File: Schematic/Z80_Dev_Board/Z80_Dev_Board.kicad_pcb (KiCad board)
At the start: 2 copper layers, 120.7 x 98.3 mm, 45 parts, among them J1 MCU Interface, J2 MCU Interface 2, J3 Expansion port, J4 UART B, J5 UART A, J6 GPIO Input, J7 GPIO Output, U1 74AC08, U2 62256, U3 62256, U4 74AC00, U5 74AC04, U6 Z80 CPU, U7 74HC157, U8 74AC74, U9 SC26C92, X1 4MHz, Y1 3,6864 MHz

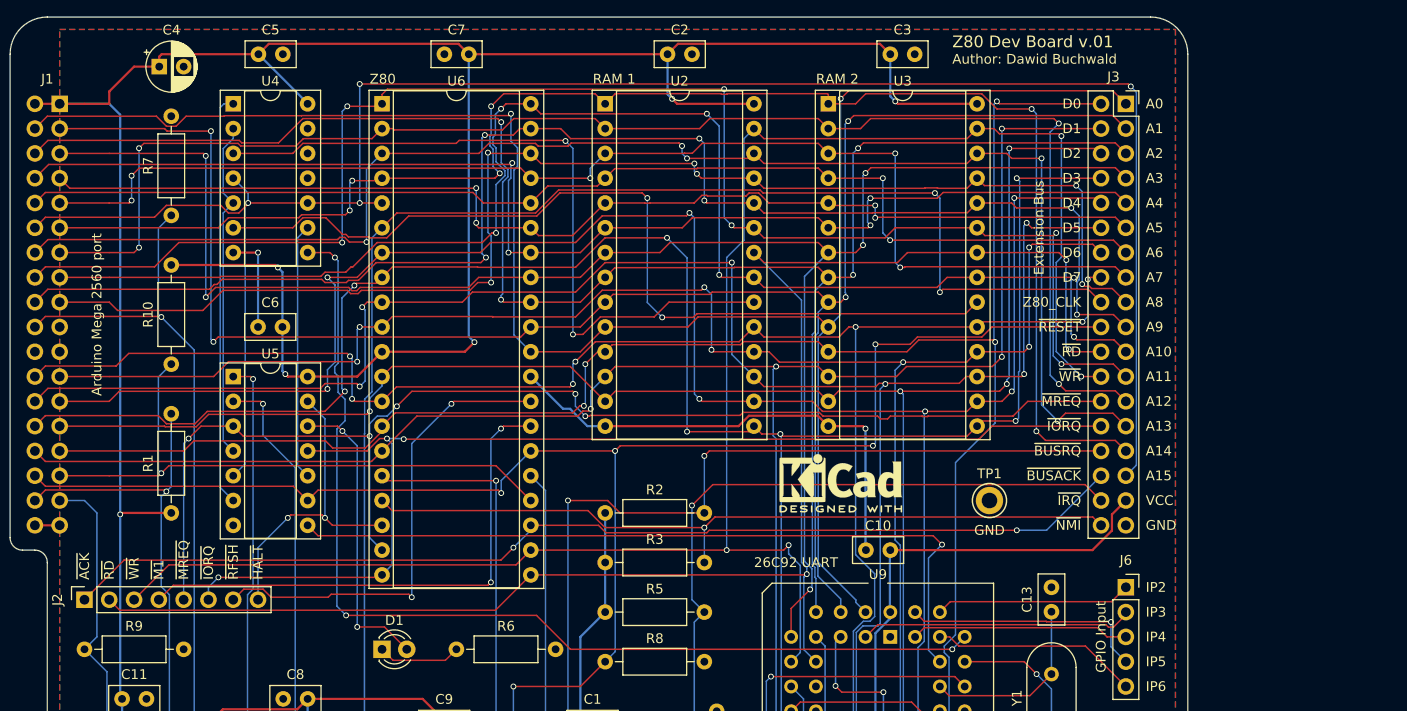
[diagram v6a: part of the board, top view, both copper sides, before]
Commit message: Started working on updated PCB with IO decoder
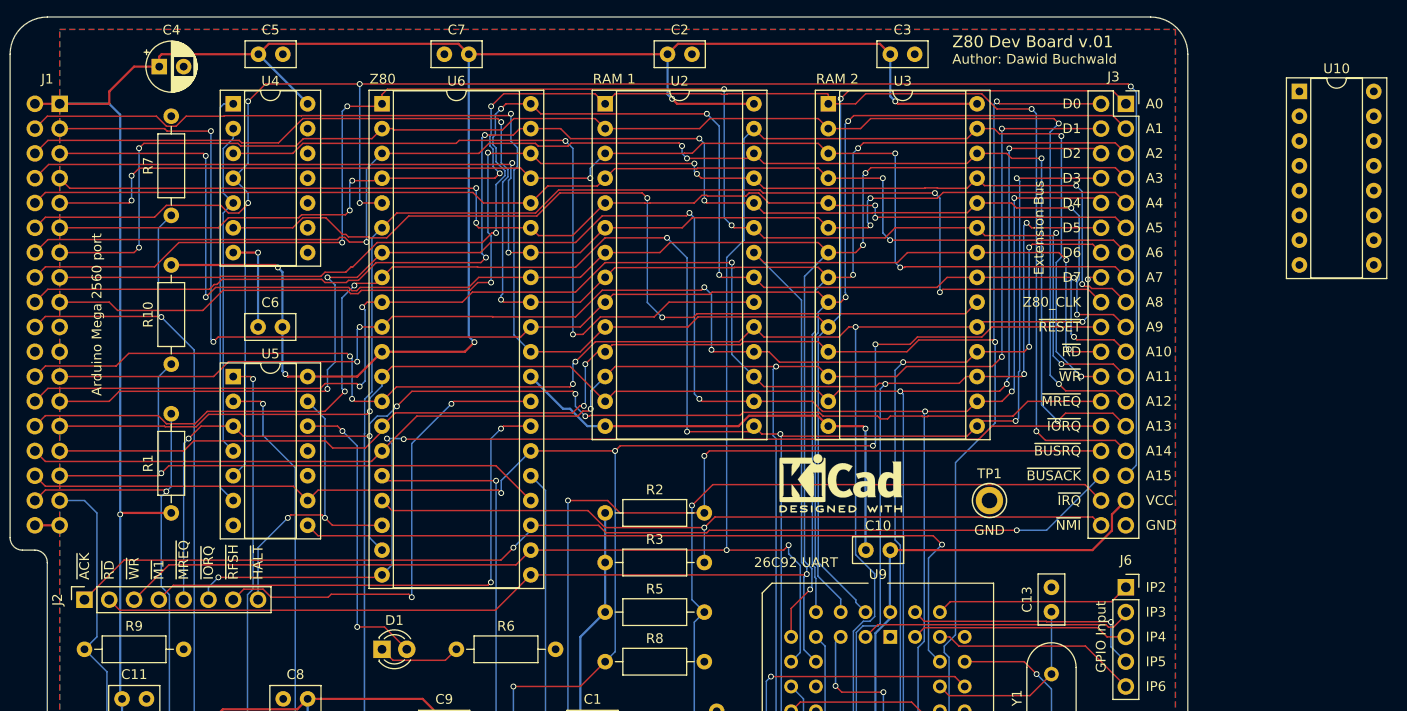
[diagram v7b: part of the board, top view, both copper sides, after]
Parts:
- added U10: 74AC138, Package_DIP:DIP-16_W7.62mm_Socket, F.Cu at (221.0, 59.7)
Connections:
- U4 pad 10: a15 -> GND
- U4 pad 8: ~UART -> Net-(U4-Pad8)
- U4 pad 9: IORQ -> GND
- U5 pad 10: IORQ -> Net-(U5-Pad10)
- U5 pad 11: ~IORQ -> GND
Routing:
- net ~UART: track 106.4 -> 0.00 mm, vias 3 -> 0
- net IORQ: track 26.3 -> 0.00 mm
- net a15: track 200.9 -> 210.2 mm, vias 4 -> 5
- net ~IORQ: track 116.6 -> 107.9 mm

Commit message: New version of the board created
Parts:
- removed the C1 at (147.3, 124.5)
- removed the C12 at (195.6, 133.3)
- removed the C2 at (156.2, 55.9)
- removed J6: GPIO Input, Connector_PinSocket_2.54mm:PinSocket_1x05_P2.54mm_Vertical
- removed J7: GPIO Output, Connector_PinSocket_2.54mm:PinSocket_1x06_P2.54mm_Vertical
- removed the R1 at (105.4, 102.9)
- removed R10, R2, R3, R4, R5, R7, R8, R9: 4K7, Resistor_THT:R_Axial_DIN0207_L6.3mm_D2.5mm_P10.16mm_Horizontal
- added C14: 22pF, Capacitor_THT:C_Disc_D5.0mm_W2.5mm_P2.50mm, F.Cu at (172.7, 102.8)
- added C3: 0,1uF, Capacitor_SMD:C_1206_3216Metric_Pad1.42x1.75mm_HandSolder, F.Cu at (104.1, 94.2)
- added C5: 0,1uF, Capacitor_SMD:C_1206_3216Metric_Pad1.42x1.75mm_HandSolder, B.Cu at (156.2, 100.3)
- added C7: 0,1uF, Capacitor_SMD:C_1206_3216Metric_Pad1.42x1.75mm_HandSolder, B.Cu at (148.6, 61.0)
- added RN1: 4K7, Resistor_THT:R_Array_SIP9, F.Cu at (119.4, 114.3)
- added RN2: 4K7, Resistor_THT:R_Array_SIP9, F.Cu at (119.4, 119.4)
- C1: renamed from C7; footprint Capacitor_THT:C_Disc_D5.0mm_W2.5mm_P2.50mm -> Capacitor_SMD:C_1206_3216Metric_Pad1.42x1.75mm_HandSolder; moved to B.Cu
- C10: footprint Capacitor_THT:C_Disc_D5.0mm_W2.5mm_P2.50mm -> Capacitor_SMD:C_1206_3216Metric_Pad1.42x1.75mm_HandSolder
- C12: renamed from C11; footprint Capacitor_THT:C_Disc_D5.0mm_W2.5mm_P2.50mm -> Capacitor_SMD:C_1206_3216Metric_Pad1.42x1.75mm_HandSolder; moved to B.Cu
- C2: renamed from C8; footprint Capacitor_THT:C_Disc_D5.0mm_W2.5mm_P2.50mm -> Capacitor_SMD:C_1206_3216Metric_Pad1.42x1.75mm_HandSolder
- C4: renamed from C9; footprint Capacitor_THT:C_Disc_D5.0mm_W2.5mm_P2.50mm -> Capacitor_SMD:C_1206_3216Metric_Pad1.42x1.75mm_HandSolder
- C6: renamed from C5; footprint Capacitor_THT:C_Disc_D5.0mm_W2.5mm_P2.50mm -> Capacitor_SMD:C_1206_3216Metric_Pad1.42x1.75mm_HandSolder
- C8: renamed from C6; footprint Capacitor_THT:C_Disc_D5.0mm_W2.5mm_P2.50mm -> Capacitor_SMD:C_1206_3216Metric_Pad1.42x1.75mm_HandSolder
- C9: renamed from C3; footprint Capacitor_THT:C_Disc_D5.0mm_W2.5mm_P2.50mm -> Capacitor_SMD:C_1206_3216Metric_Pad1.42x1.75mm_HandSolder; moved to B.Cu
- J3: value Expansion port -> UART B; footprint Connector_PinSocket_2.54mm:PinSocket_2x18_P2.54mm_Vertical -> Connector_PinHeader_2.54mm:PinHeader_1x06_P2.54mm_Horizontal
- J4: value UART B -> UART A
- J5: value UART A -> Extension Bus; footprint Connector_PinHeader_2.54mm:PinHeader_1x06_P2.54mm_Horizontal -> Connector_PinSocket_2.54mm:PinSocket_2x32_P2.54mm_Vertical
- U1: renamed from U8; footprint Package_DIP:DIP-14_W7.62mm_Socket -> Package_SO:SOIC-14_3.9x8.7mm_P1.27mm
- U10: value 74AC138 -> SC26C92; footprint Package_DIP:DIP-16_W7.62mm_Socket -> Package_LCC:PLCC-44_THT-Socket
- U2: renamed from U5; footprint Package_DIP:DIP-14_W7.62mm_Socket -> Package_SO:SOIC-14_3.9x8.7mm_P1.27mm
- U4: footprint Package_DIP:DIP-14_W7.62mm_Socket -> Package_SO:SOIC-14_3.9x8.7mm_P1.27mm
- U5: renamed from U2; value 62256 -> 71256; footprint Package_DIP:DIP-28_W15.24mm_Socket -> Package_DIP:DIP-28_W7.62mm_Socket
- U6: renamed from U1; footprint Package_DIP:DIP-14_W7.62mm_Socket -> Package_SO:SOIC-14_3.9x8.7mm_P1.27mm
- U7: renamed from U3; value 62256 -> 71256; footprint Package_DIP:DIP-28_W15.24mm_Socket -> Package_DIP:DIP-28_W7.62mm_Socket
- U8: renamed from U7; footprint Package_DIP:DIP-16_W7.62mm_Socket -> Package_SO:SOIC-16_3.9x9.9mm_P1.27mm
- U9: value SC26C92 -> 74AC138; footprint Package_LCC:PLCC-44_THT-Socket -> Package_SO:SOIC-16_3.9x9.9mm_P1.27mm
- moved J5 80.7 mm to (184.2, 58.4), turned to 0 degrees
- moved U10 78.2 mm to (157.5, 105.4)
- moved TP1 78.2 mm to (113.0, 119.4)
- moved J3 76.7 mm to (166.4, 128.3), turned to 270 degrees
- moved U9 57.4 mm to (124.5, 133.3)
- moved C10 55.1 mm to (124.5, 124.5)
- moved C4 49.3 mm to (104.1, 83.8), turned to 90 degrees
- moved J4 49.3 mm to (146.1, 128.3)
- moved U1 49.1 mm to (111.8, 83.8), turned to 90 degrees
- moved U6 48.5 mm to (111.8, 94.0), turned to 90 degrees
- moved REF** 32.6 mm to (172.7, 134.6)
- moved C1 31.4 mm to (125.7, 86.4), turned to 180 degrees
- moved R1 31.2 mm to (106.7, 102.9)
- moved D1 30.1 mm to (100.3, 102.9)
- moved REF** 27.5 mm to (172.7, 72.4), turned to 90 degrees
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- renumbered C4 to C11, R6 to R1, U6 to U3
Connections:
- C10 pad 1: GND -> +5V
- C10 pad 2: +5V -> GND
- C13 pad 1: Net-(C13-Pad1) -> GND
- C13 pad 2: GND -> Net-(C13-Pad2)
- J1 pad 19: Net-(J1-Pad19) -> /ports/mc1
- J1 pad 21: Net-(J1-Pad21) -> /ports/mc2
- J1 pad 22: Net-(J1-Pad22) -> /ports/mc3
- J3 pad 1: a0 -> GND
- J3 pad 2: d0 -> UARTB_~RTS
- J3 pad 3: a1 -> (no net)
- J3 pad 4: d1 -> UARTB_RxD
- J3 pad 5: a2 -> UARTB_TxD
- J3 pad 6: d2 -> UARTB_~CTS
- J4 pad 2: UARTB_~RTS -> UARTA_~RTS
- J4 pad 3: Net-(J4-Pad3) -> (no net)
- J4 pad 4: UARTB_RxD -> UARTA_RxD
- J4 pad 5: UARTB_TxD -> UARTA_TxD
- J4 pad 6: UARTB_~CTS -> UARTA_~CTS
- J5 pad 1: GND -> +5V
- J5 pad 2: UARTA_~RTS -> +5V
- J5 pad 3: Net-(J5-Pad3) -> GND
- J5 pad 4: UARTA_RxD -> GND
- J5 pad 5: UARTA_TxD -> a0
- J5 pad 6: UARTA_~CTS -> d0
- U1 pad 6: Net-(U8-Pad6) -> (no net)
- U1 pad 8: Net-(U8-Pad8) -> (no net)
- U10 pad 1: a5 -> (no net)
- U10 pad 10: Net-(U10-Pad10) -> ~RD
- U10 pad 11: Net-(U10-Pad11) -> UARTB_RxD
- U10 pad 12: Net-(U10-Pad12) -> (no net)
- U10 pad 13: Net-(U10-Pad13) -> UARTB_TxD
- U10 pad 14: Net-(U10-Pad14) -> UARTB_~RTS
- U10 pad 15: ~UART -> /ports/op3
- U10 pad 16: +5V -> /ports/op5
- U10 pad 2: a6 -> a0
- U10 pad 3: a7 -> /ports/ip3
- U10 pad 4: ~IORQ -> a1
- U10 pad 5: ~IORQ -> UARTB_~CTS
- U10 pad 6: +5V -> a2
- U10 pad 7: Net-(U10-Pad7) -> a3
- U10 pad 8: GND -> UARTA_~CTS
- U10 pad 9: Net-(U10-Pad9) -> ~WR
- U2 pad 10: Net-(U5-Pad10) -> (no net)
- U4 pad 11: Net-(U4-Pad11) -> (no net)
- U4 pad 8: Net-(U4-Pad8) -> (no net)
- U6 pad 11: Net-(U1-Pad11) -> (no net)
- U6 pad 8: Net-(U1-Pad8) -> (no net)
- U8 pad 12: Net-(U7-Pad12) -> (no net)
- U8 pad 7: Net-(U7-Pad7) -> (no net)
- U8 pad 9: Net-(U7-Pad9) -> (no net)
- U9 pad 1: Net-(U9-Pad1) -> a5
- U9 pad 10: ~RD -> ~IO5
- U9 pad 11: UARTB_RxD -> ~IO4
- U9 pad 12: Net-(U9-Pad12) -> ~IO3
- U9 pad 13: UARTB_TxD -> ~IO2
- U9 pad 14: UARTB_~RTS -> ~IO1
- U9 pad 15: /ports/op3 -> ~UART
- U9 pad 16: /ports/op5 -> +5V
- U9 pad 2: a0 -> a6
- U9 pad 3: /ports/ip3 -> a7
- U9 pad 4: a1 -> ~IORQ
- U9 pad 5: UARTB_~CTS -> ~IORQ
- U9 pad 6: a2 -> +5V
- U9 pad 7: a3 -> ~IO7
- U9 pad 8: UARTA_~CTS -> GND
- U9 pad 9: ~WR -> ~IO6
- X1 pad 1: Net-(X1-Pad1) -> (no net)
- Y1 pad 1: Net-(C12-Pad2) -> Net-(C13-Pad2)
- Y1 pad 2: Net-(C13-Pad1) -> Net-(C14-Pad1)
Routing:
- net GND: track 87.9 -> 252.3 mm, vias 2 -> 22
- net /ports/mc1: track 0.00 -> 137.8 mm, vias 0 -> 2
- net /ports/mc3: track 0.00 -> 133.8 mm, vias 0 -> 1
- net /ports/mc2: track 0.00 -> 130.4 mm, vias 0 -> 1
- net a15: track 210.2 -> 135.3 mm, vias 5 -> 3
- net ~IO1: track 0.00 -> 67.7 mm
- net ~IO2: track 0.00 -> 67.0 mm
- net ~IO7: track 0.00 -> 66.1 mm
- net a7: track 127.0 -> 192.3 mm, vias 5 -> 4
- net a6: track 121.0 -> 186.3 mm, vias 2 -> 4
- net ~IO3: track 0.00 -> 65.3 mm
- net ~IO4: track 0.00 -> 63.5 mm
- net ~UART: track 0.00 -> 63.2 mm, vias 0 -> 1
- net ~IO5: track 0.00 -> 61.8 mm
- net ~IO6: track 0.00 -> 61.3 mm
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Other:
- board size 120.7 x 98.3 mm -> 101.6 x 83.8 mm
- board text added: "MC1"
- board text added: "MC2"
- board text added: "MC3"
- board text added: "N/C"
- board text added: "Z80 CPU"
- board text added: "Z80 Development Board v.02"
- board text added: "~BSACK"
- board text added: "~IO1"
- board text added: "~IO2"
- board text added: "~IO3"
- board text added: "~IO4"
- board text added: "~IO5"
- board text added: "~IO6"
- board text added: "~IO7"
- board text removed: "Arduino Mega 2560 port"
- board text removed: "GPIO Input"
- board text removed: "GPIO Output"
- board text removed: "Z80"
- board text removed: "Z80 Dev Board v.01"
- board text removed: "~BUSACK"
